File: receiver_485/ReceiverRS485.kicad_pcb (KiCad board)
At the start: 2 copper layers, 160 x 100.1 mm, 94 parts, among them J1 USB3_A, J2 Conn_01x03, J3 USB3_A, J4 Conn_01x03, J5 USB3_A, J6 Conn_01x03, J7 USB3_A, J8 Conn_01x03, U1 RFM-0505S, U10 MAX3283E, U11 TLP2372, U12 TLP2372, U13 RFM-0505S, U14 MAX3283E, U15 TLP2372, U16 MAX3283E, U17 TLP2372, U18 TLP2372, U19 RFM-0505S, U2 MAX3283E, U20 MAX3283E, U21 TLP2372, U22 MAX3283E, U23 TLP2372, U24 TLP2372, U25 USB3_duplo, U26 USB3_duplo, U3 TLP2372, U4 MAX3283E, U5 TLP2372, U6 TLP2372, U7 RFM-0505S, U8 MAX3283E, U9 TLP2372

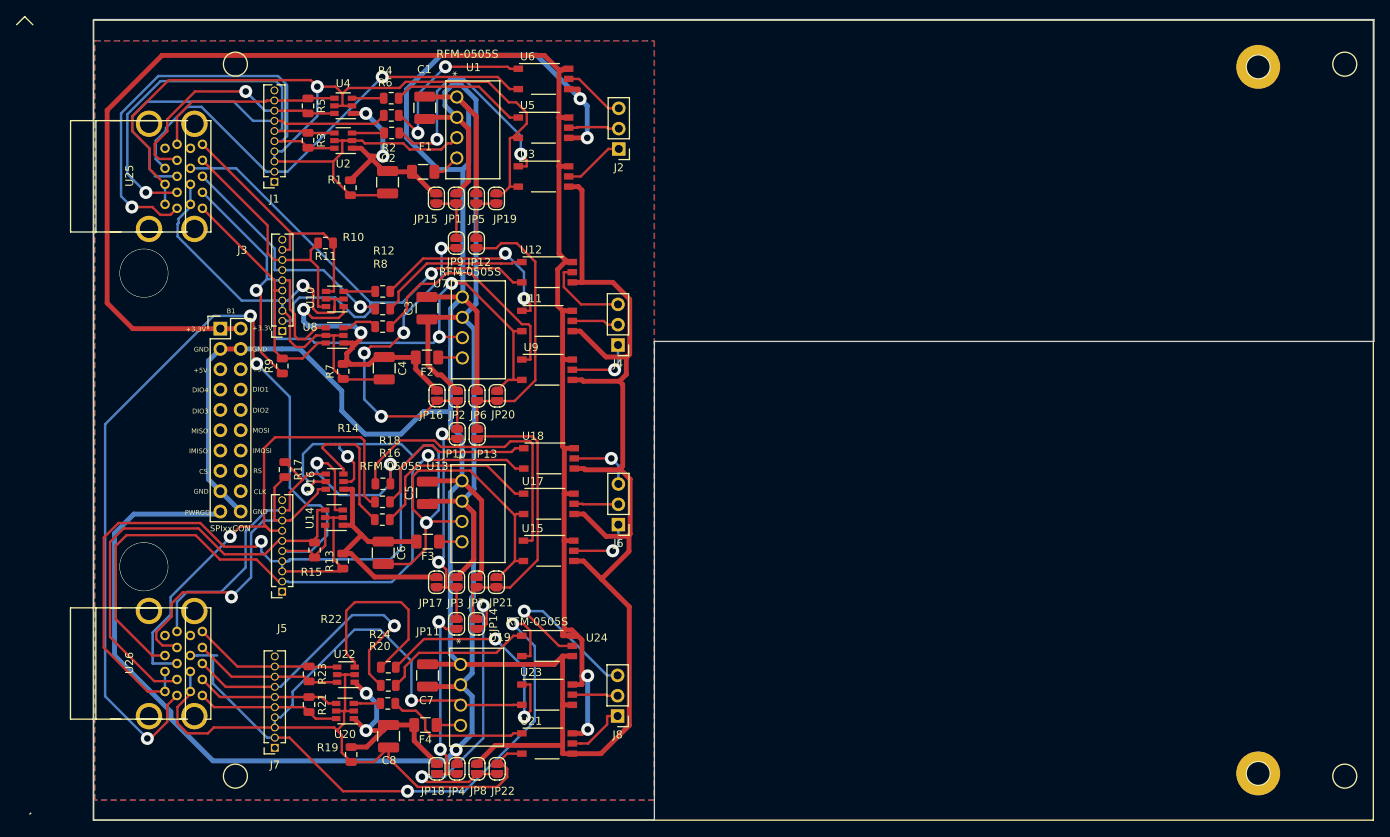
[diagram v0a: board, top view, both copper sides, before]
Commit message: Changed version of SPIxxcCON BUS
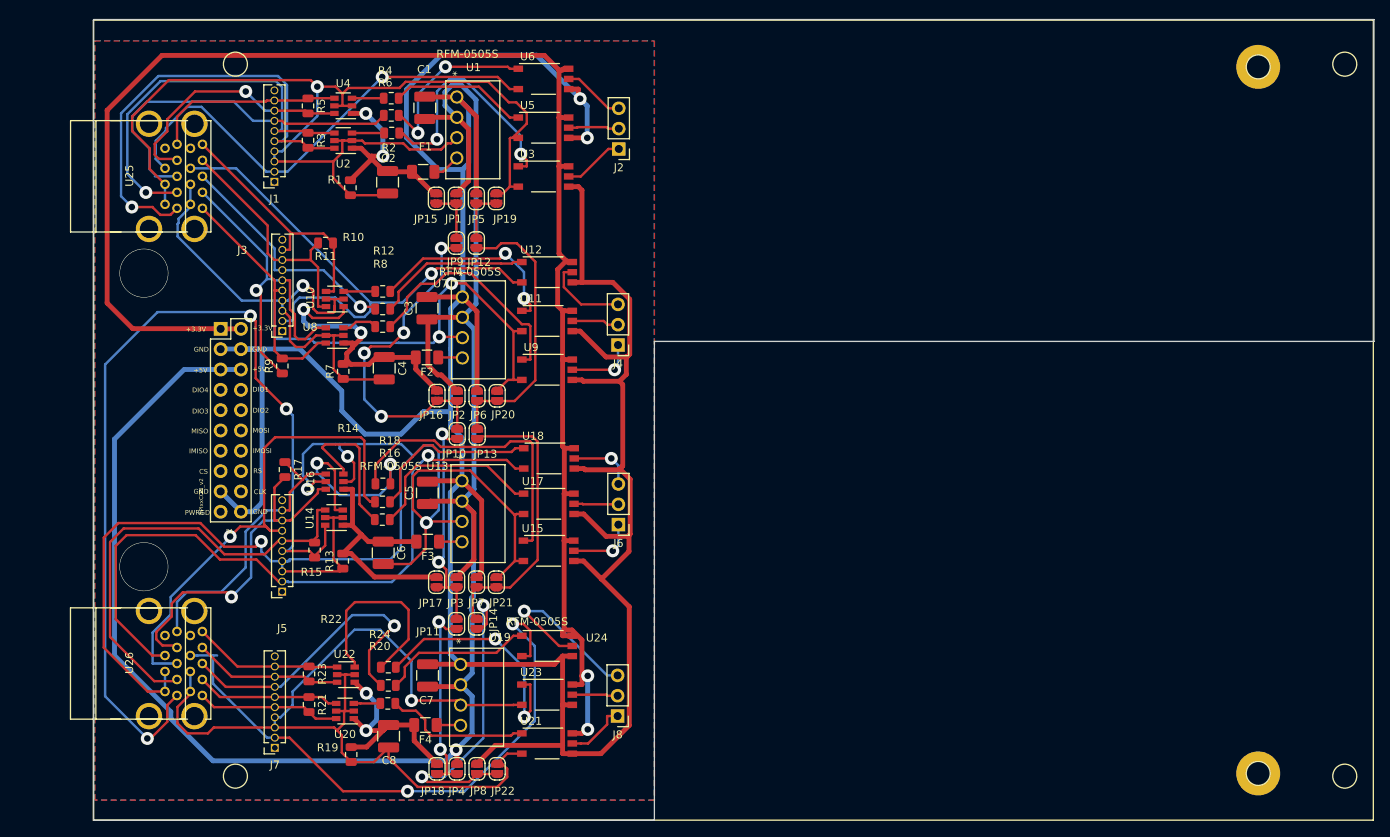
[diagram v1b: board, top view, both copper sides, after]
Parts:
- B1: value SPIxxCON -> SPIxxCON_v2; footprint Pin_Headers:Pin_Header_Straight_2x10 -> Controle:SPIxxCON_(only_connector)
- moved B1 11.5 mm to (119.9, 93.2)
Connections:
- B1 pad 19: +5V -> Net-(B1-Pad19)
- B1 pad 5: Net-(B1-Pad5) -> +5V
- B1 pad 6: Net-(B1-Pad6) -> +5V
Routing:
- net +5V: track 225.2 -> 241.9 mm
- net GND: track 399.5 -> 405.3 mm
- net ssrx-_ch3: track 120.1 -> 118.6 mm

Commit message: Arrumado Silk screen
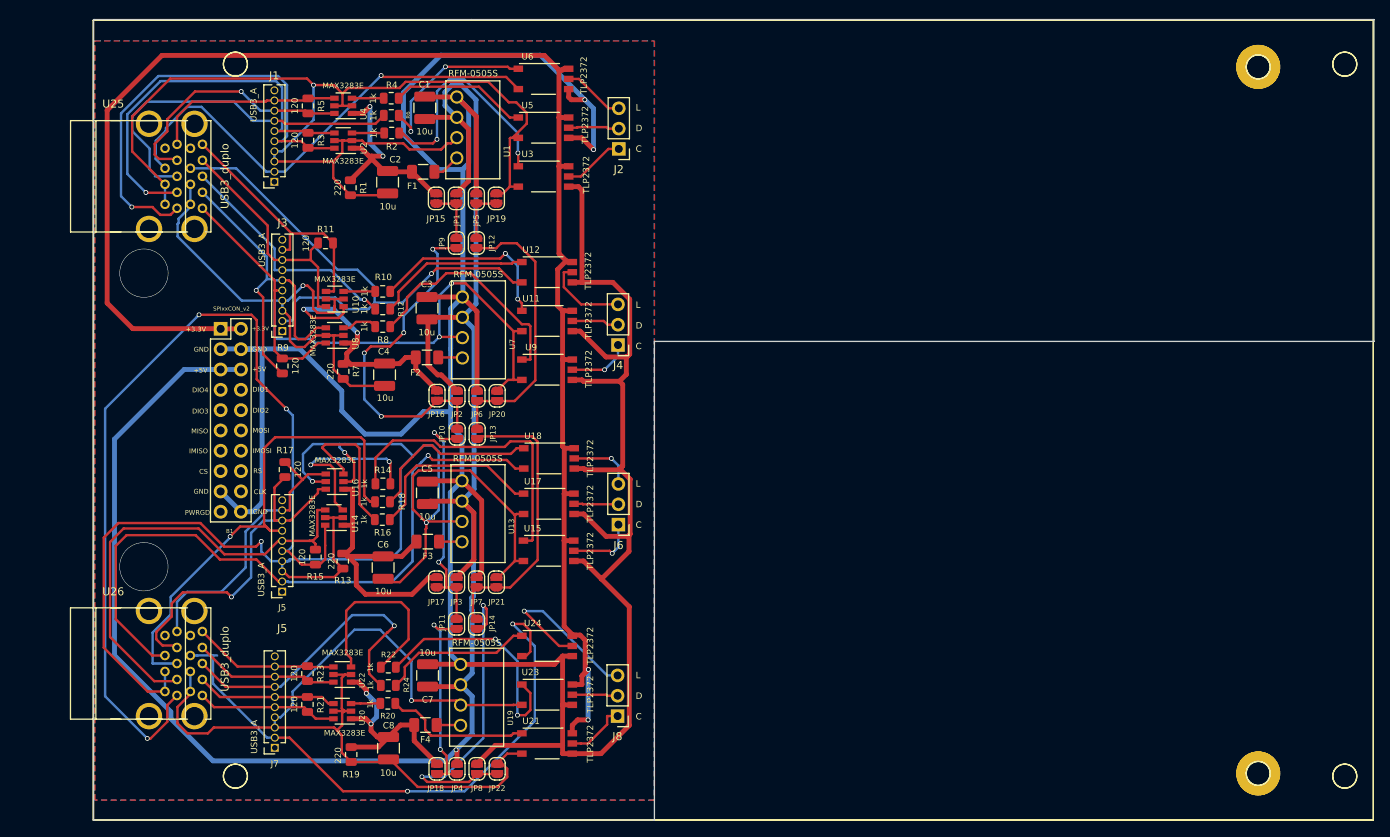
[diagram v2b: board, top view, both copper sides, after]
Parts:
- added  : C64AC, Controle:Eurocard_template_editado, F.Cu at (262.7, 143.1)
- moved C6 1.85 mm to (138.9, 111.6)
- moved C8 1.50 mm to (139.6, 134.2)
- moved R15 0.88 mm to (130.5, 110.3)
- moved C4 0.81 mm to (139.1, 87.5)
- moved U22 0.46 mm to (133.8, 124.9)
- moved U20 0.35 mm to (133.8, 129.5)
- moved R23 0.20 mm to (129.5, 124.8)
- moved R21 0.20 mm to (129.5, 128.7)
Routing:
- net ch3+5: track 32.0 -> 37.3 mm
- net GND: track 405.3 -> 409.7 mm
- net Net-(R14-Pad1): track 25.5 -> 21.8 mm
- net D+_ch4: track 118.7 -> 116.6 mm
- net ssrx+_ch3: track 56.1 -> 57.8 mm
- net ssrx-_ch3: track 118.6 -> 117.0 mm
- net Net-(JP10-Pad2): track 28.4 -> 30.1 mm
- net ch1+5: track 26.2 -> 27.7 mm
- net Net-(R10-Pad2): track 25.9 -> 24.4 mm
- net Net-(R2-Pad2): track 30.7 -> 29.2 mm
- net ch4+5: track 28.0 -> 29.5 mm
- net ch2+5: track 37.1 -> 36.0 mm
- net Net-(JP10-Pad1): track 42.9 -> 44.0 mm
- net /CHANNEL_2/CLK: track 8.56 -> 7.82 mm
- net +3V3: track 205.1 -> 204.5 mm
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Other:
- board text added: "L D C"
